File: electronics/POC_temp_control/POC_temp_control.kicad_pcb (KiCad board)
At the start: 2 copper layers, 109.2 x 78.7 mm, 177 parts, among them J1 Conn_01x02, J2 Conn_01x07, J3 Conn_01x05, J4 Conn_01x06, J5 Conn_01x02, J6 Conn_01x02, Q1 PXT8050, Q2 PXT8050, Q3 PXT8550, Q4 Q_PMOS_DUAL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

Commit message: straggling changes
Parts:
- D15: value BZX84C18 -> BZT52C18; footprint SquantorIC:SOT23-3 -> SquantorDiodes:SOD-323-nexperia-hand
- D16: value BAV70 -> BZT52C18; footprint SquantorIC:SOT23-3 -> SquantorDiodes:SOD-323-nexperia-hand
- D17: value BAS16 -> BAV70
- D18: value BZX84C18 -> BAV70
- D19: value BAV70 -> BAS316; footprint SquantorIC:SOT23-3 -> SquantorDiodes:SOD-323-nexperia-hand
- D20: value BAS16 -> BAS316; footprint SquantorIC:SOT23-3 -> SquantorDiodes:SOD-323-nexperia-hand
- Q5: value BC858B -> Q_PMOS_DUAL; footprint SquantorIC:SOT23-3 -> SquantorIC:SOIC-8
- Q6: value BC847A -> BC858B
- Q7: value Q_PMOS_DUAL -> BC858B; footprint SquantorIC:SOIC-8 -> SquantorIC:SOT23-3
- Q8: value BC858B -> BC847A
- R57: value 5K6 -> 10M
- R58: value 1M -> 5K6
- R59: value 1K5 -> 1M
- R60: value 2K2 -> 5K6
- R61: value 330 -> 1M
- R62: value 330 -> 1K5
- R63: value 6K8 -> 1K5
- R64, R65: value 10K -> 2K2
- R66: value 10K -> 330
- R67: value 10M -> 330
- R68: value 5K6 -> 330
- R69: value 1M -> 330
- R70: value 1K5 -> 6K8
- R71: value 2K2 -> 6K8
- R72, R73: value 330 -> 10K
- R74: value 6K8 -> 10K
- moved JP2 195.1 mm to (45.8, 40.5)
- moved OP1 194.9 mm to (48.1, 50.3), turned to 90 degrees
- moved C30 192.0 mm to (45.4, 44.1), turned to 90 degrees
- moved JP1 191.5 mm to (45.8, 36.9)
- moved OP2 189.8 mm to (52.9, 50.3), turned to 90 degrees
- moved R64 186.9 mm to (45.4, 47.3), turned to -90 degrees
- moved R66 181.9 mm to (50.5, 53.1), turned to -90 degrees
- moved R33 180.1 mm to (47.9, 36.5), turned to 90 degrees
- moved Q4 179.7 mm to (51.4, 38.9), turned to 90 degrees
- moved Q6 177.8 mm to (46.4, 56.3), turned to 90 degrees
- moved R62 177.5 mm to (50.5, 47.5), turned to 90 degrees
- moved R58 174.7 mm to (53.4, 45.4)
- moved R59 174.6 mm to (53.4, 43.4)
- moved R65 172.3 mm to (59.9, 46.9), turned to -90 degrees
- moved D15 171.9 mm to (47.4, 44.2), turned to 90 degrees
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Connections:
- net /Power control/AC_P1 renamed /AC_P1
- C30 pad 2: /Power control/SW_S1 -> /SW_S1
- C31 pad 1: Net-(D18-K) -> Net-(D16-K)
- C31 pad 2: /Power control/SW_S2 -> /SW_S2
- D15 pad 1: /Power control/SW_S1 -> Net-(D15-K)
- D15 pad 2: (no net) -> /SW_S1
- D16 pad 1: /Power control/SW_S1 -> Net-(D16-K)
- D16 pad 2: Net-(D16-K2) -> /SW_S2
- D17 pad 1: /Power control/GND -> /SW_S1
- D17 pad 2: (no net) -> Net-(D17-K2)
- D17 pad 3: Net-(D17-K) -> /SW_G1
- D18 pad 1: /Power control/SW_S2 -> /SW_S2
- D18 pad 2: (no net) -> Net-(D18-K2)
- D18 pad 3: Net-(D18-K) -> /SW_G2
- D19 pad 1: /Power control/SW_S2 -> Net-(D19-K)
- D19 pad 2: Net-(D19-K2) -> /GND
- D20 pad 1: /Power control/GND -> Net-(D20-K)
- D20 pad 2: (no net) -> /GND
- JP1 pad 1: /Power control/AC2 -> /AC2
- JP2 pad 1: /Power control/AC1 -> /AC1
- JP3 pad 1: /Power control/AC2 -> /AC2
- JP3 pad 2: /Power control/AC_P2 -> /AC_P2
- JP4 pad 1: /Power control/AC1 -> /AC1
- JP4 pad 2: /Power control/AC_P2 -> /AC_P2
- OP1 pad 1: Net-(Q5-C) -> Net-(Q6-C)
- OP2 pad 2: Net-(Q6-C) -> Net-(Q8-C)
- OP2 pad 3: /Power control/SW_S1 -> /SW_S1
- OP2 pad 4: Net-(D16-K2) -> Net-(D17-K2)
- OP3 pad 1: Net-(Q8-C) -> Net-(Q7-C)
- OP3 pad 4: Net-(D18-K) -> Net-(D16-K)
- OP4 pad 3: /Power control/SW_S2 -> /SW_S2
- OP4 pad 4: Net-(D19-K2) -> Net-(D18-K2)
- Q4 pad 2: /Power control/SW_G1 -> /SW_G1
- Q4 pad 3: /Power control/COM1 -> /COM1
- Q4 pad 4: /Power control/SW_G1 -> /SW_G1
- Q4 pad 5: /Power control/SW_S1 -> /SW_S1
- Q4 pad 6: /Power control/SW_S1 -> /SW_S1
- Q4 pad 7: /Power control/SW_S1 -> /SW_S1
- Q4 pad 8: /Power control/SW_S1 -> /SW_S1
- Q5 pad 1: Net-(Q5-B) -> /AC_P2
- Q5 pad 2: /Power control/VD3.3V+ -> /SW_G2
- Q5 pad 3: Net-(Q5-C) -> /COM1
- Q6 pad 2: /Power control/GND -> /VD3.3V+
- Q7 pad 1: /Power control/AC_P2 -> Net-(Q7-B)
- Q7 pad 2: /Power control/SW_G2 -> /VD3.3V+
- Q7 pad 3: /Power control/COM1 -> Net-(Q7-C)
- Q8 pad 2: /Power control/VD3.3V+ -> /GND
- Q9 pad 2: /Power control/GND -> /GND
- R33 pad 2: /Power control/COM1 -> /COM1
- R57 pad 1: /Power control/SW_G1 -> /AC_P2
- R57 pad 2: Net-(D16-K2) -> /COM1
- R58 pad 1: /Power control/SW_G1 -> /SW_G1
- R58 pad 2: /Power control/SW_S1 -> Net-(D17-K2)
- R59 pad 1: Net-(OP1-Pad3) -> /SW_G1
- R59 pad 2: Net-(D16-K2) -> /SW_S1
- R60 pad 1: Net-(D15-K) -> /SW_G2
- R60 pad 2: Net-(D17-K) -> Net-(D18-K2)
- R61 pad 1: /Power control/GND -> /SW_G2
- R61 pad 2: Net-(OP1-Pad2) -> /SW_S2
- R62 pad 1: Net-(OP2-Pad1) -> Net-(OP1-Pad3)
- R62 pad 2: /Power control/VD3.3V+ -> Net-(D17-K2)
- R63 pad 1: Net-(Q5-B) -> Net-(OP3-Pad3)
- R63 pad 2: /Power control/VD3.3V+ -> Net-(D18-K2)
- R64 pad 1: Net-(Q5-B) -> Net-(D15-K)
- R64 pad 2: /Power control/SW_LOAD_1 -> Net-(D19-K)
- R65 pad 1: Net-(Q6-B) -> Net-(D16-K)
- R65 pad 2: /Power control/SW_LOAD_1 -> Net-(D20-K)
- R66 pad 1: /Power control/SW_LOAD_1 -> /GND
- R66 pad 2: /Power control/VD3.3V+ -> Net-(OP1-Pad2)
- R67 pad 1: /Power control/AC_P2 -> Net-(OP2-Pad1)
- R67 pad 2: /Power control/COM1 -> /VD3.3V+
- R68 pad 1: /Power control/SW_G2 -> /GND
- R68 pad 2: Net-(D19-K2) -> Net-(OP3-Pad2)
- R69 pad 1: /Power control/SW_G2 -> Net-(OP4-Pad1)
- R69 pad 2: /Power control/SW_S2 -> /VD3.3V+
- R70 pad 1: Net-(OP3-Pad3) -> Net-(Q6-B)
- R70 pad 2: Net-(D19-K2) -> /VD3.3V+
- R71 pad 1: Net-(D18-K) -> Net-(Q7-B)
- R71 pad 2: Net-(D20-K) -> /VD3.3V+
- R72 pad 1: /Power control/GND -> Net-(Q6-B)
- R72 pad 2: Net-(OP3-Pad2) -> /SW_LOAD_1
- R73 pad 1: Net-(OP4-Pad1) -> Net-(Q8-B)
- R73 pad 2: /Power control/VD3.3V+ -> /SW_LOAD_1
- R74 pad 1: Net-(Q8-B) -> Net-(Q7-B)
- R74 pad 2: /Power control/VD3.3V+ -> /SW_LOAD_2
- R75 pad 1: Net-(Q8-B) -> Net-(Q9-B)
- R75 pad 2: /Power control/SW_LOAD_2 -> /SW_LOAD_2
- R76 pad 1: Net-(Q9-B) -> /SW_LOAD_1
- R76 pad 2: /Power control/SW_LOAD_2 -> /VD3.3V+
- R77 pad 1: /Power control/SW_LOAD_2 -> /SW_LOAD_2
- R77 pad 2: /Power control/VD3.3V+ -> /VD3.3V+

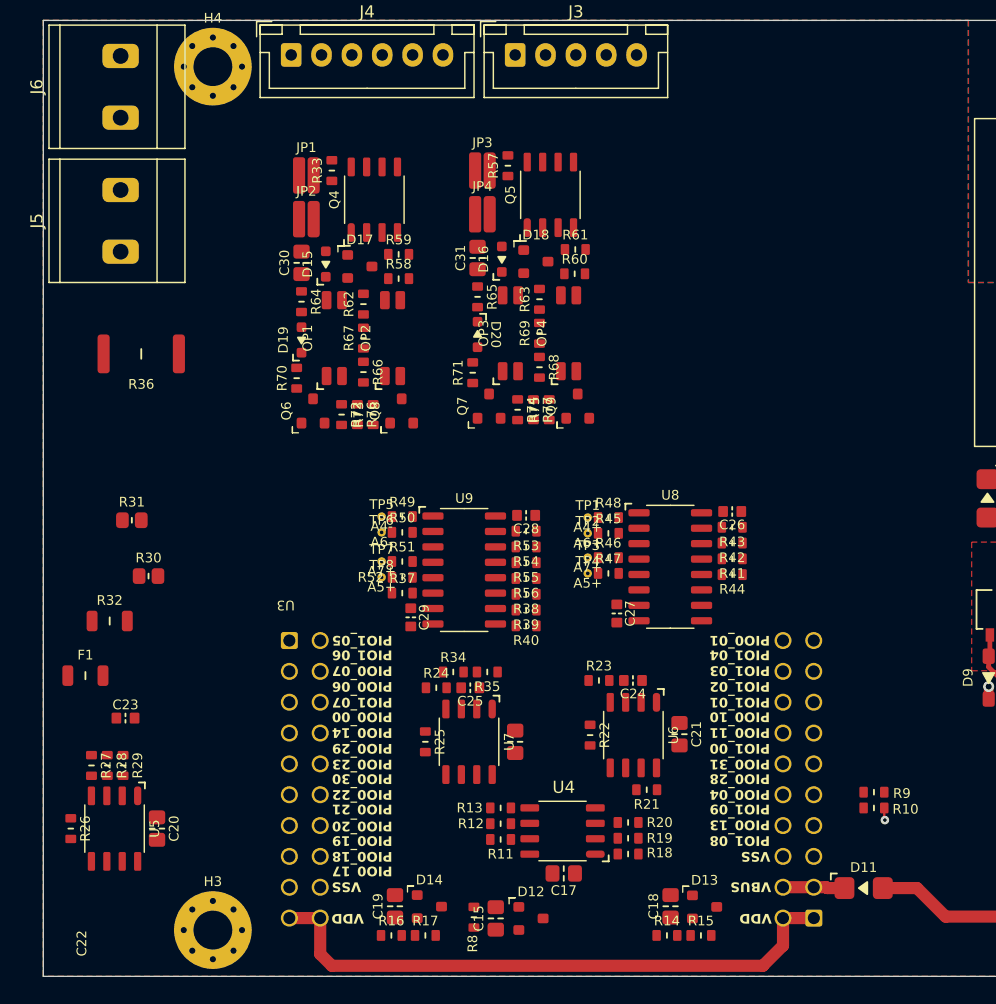
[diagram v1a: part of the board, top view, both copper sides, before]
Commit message: replaced current sense resistor, imported zerocross detector
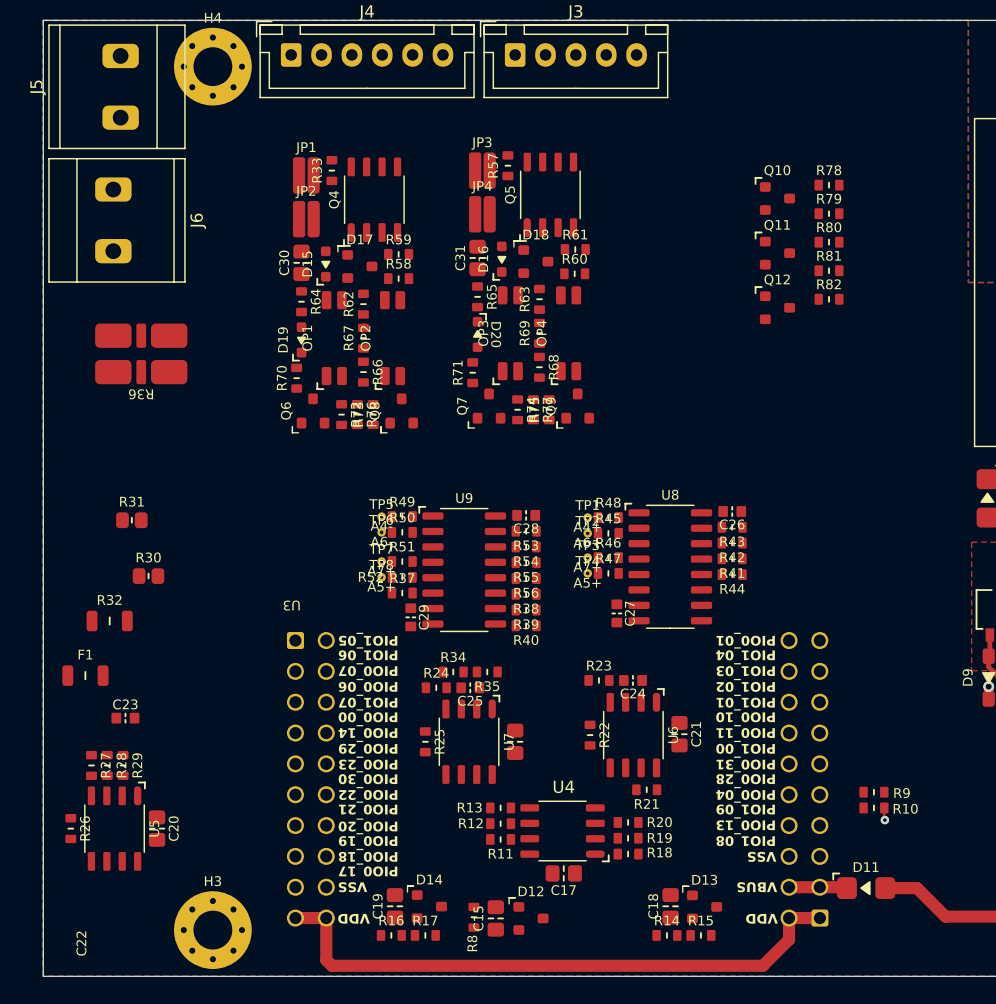
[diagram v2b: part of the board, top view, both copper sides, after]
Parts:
- added Q10: BC847A, SquantorIC:SOT23-3, F.Cu at (84.6, 38.8)
- added Q11: BC858B, SquantorIC:SOT23-3, F.Cu at (84.6, 43.3)
- added Q12: BC847A, SquantorIC:SOT23-3, F.Cu at (84.6, 47.8)
- added R78: 47K, SquantorResistor:R_0603_hand, F.Cu at (88.8, 37.7)
- added R79: 10K, SquantorResistor:R_0603_hand, F.Cu at (88.8, 40.0)
- added R80: 10K, SquantorResistor:R_0603_hand, F.Cu at (88.8, 42.4)
- added R81: 22K, SquantorResistor:R_0603_hand, F.Cu at (88.8, 44.8)
- added R82: 1M, SquantorResistor:R_0603_hand, F.Cu at (88.8, 47.1)
- R36: footprint SquantorResistor:R_2512 -> SquantorResistor:R_1225_kelvin
- moved J5 11.0 mm to (30.5, 29.6)
- moved J6 11.0 mm to (29.9, 40.6), turned to -90 degrees
- moved U3 0.50 mm to (66.5, 87.0)
- moved D11 0.20 mm to (91.9, 95.6)
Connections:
- Q5 pad 3: /COM1 -> /COM2
- R36 pad 2: /GND -> unconnected-(R36-Pad2)
- R57 pad 2: /COM1 -> /COM2

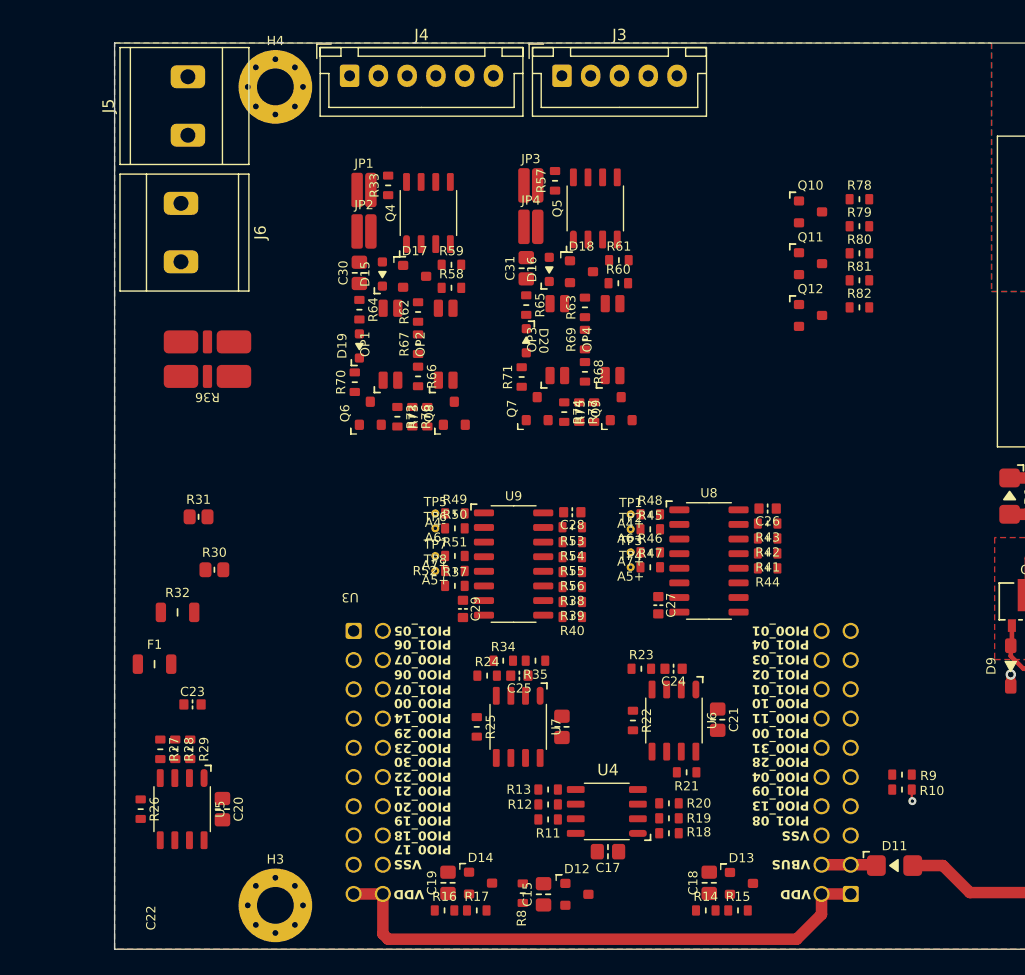
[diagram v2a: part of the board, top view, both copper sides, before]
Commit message: more schematic bits added, passes ERC, placing components and fixing silk orientations
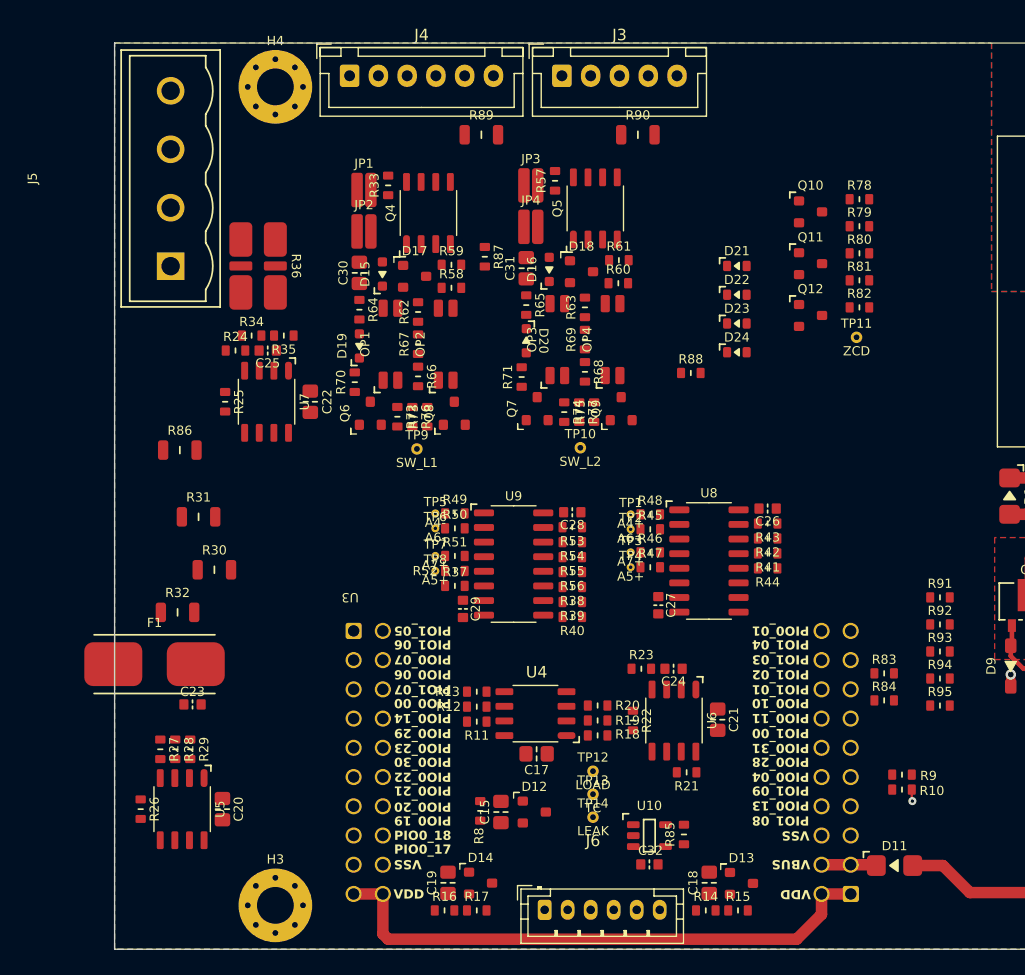
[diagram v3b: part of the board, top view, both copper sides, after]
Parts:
- added C32: 1u, SquantorCapacitor:C_0603, F.Cu at (70.6, 95.5)
- added D21: Yel, SquantorDiodes:LED_0603_hand, F.Cu at (78.2, 43.5)
- added D22: blu, SquantorDiodes:LED_0603_hand, F.Cu at (78.2, 46.0)
- added D23: blu, SquantorDiodes:LED_0603_hand, F.Cu at (78.2, 48.5)
- added D24: Yel, SquantorDiodes:LED_0603_hand, F.Cu at (78.2, 51.0)
- added R83: 3K3, SquantorResistor:R_0603_hand, F.Cu at (91.0, 78.9)
- added R84: 3K3, SquantorResistor:R_0603_hand, F.Cu at (91.0, 81.2)
- added R85: 4K7, SquantorResistor:R_0603_hand, F.Cu at (73.6, 92.9)
- added R86: 0R, SquantorResistor:R_1206, F.Cu at (29.8, 59.5)
- added R87: 10k, SquantorResistor:R_0603_hand, F.Cu at (56.3, 42.7)
- added R88: 10k, SquantorResistor:R_0603_hand, F.Cu at (74.2, 52.8)
- added R89: 0R, SquantorResistor:R_1206, F.Cu at (56.0, 32.1)
- added R90: 0R, SquantorResistor:R_1206, F.Cu at (69.6, 32.1)
- added R91: 10K, SquantorResistor:R_0603_hand, F.Cu at (95.8, 72.3)
- added R92: 10K, SquantorResistor:R_0603_hand, F.Cu at (95.8, 74.7)
- added R93: 10K, SquantorResistor:R_0603_hand, F.Cu at (95.8, 77.0)
- added R94: 10K, SquantorResistor:R_0603_hand, F.Cu at (95.8, 79.3)
- added R95: 10K, SquantorResistor:R_0603_hand, F.Cu at (95.8, 81.7)
- added TP10: SW_L2, SquantorTestPoints:TestPoint_hole_H05R10, F.Cu at (64.6, 59.3)
- added TP11: ZCD, SquantorTestPoints:TestPoint_hole_H05R10, F.Cu at (88.6, 49.7)
- added TP12: LOAD, SquantorTestPoints:TestPoint_hole_H05R10, F.Cu at (65.7, 87.4)
- added TP13: TC, SquantorTestPoints:TestPoint_hole_H05R10, F.Cu at (65.7, 89.4)
- added TP14: LEAK, SquantorTestPoints:TestPoint_hole_H05R10, F.Cu at (65.7, 91.4)
- added TP9: SW_L1, SquantorTestPoints:TestPoint_hole_H05R10, F.Cu at (50.4, 59.4)
- added U10: ~, SquantorIC:SOT23-5-Microchip-OT, F.Cu at (70.6, 93.0)
- F1: footprint SquantorResistor:R_1206 -> SquantorFuse:FH_XF-155
- J5: value Conn_01x02 -> Conn_01x04; footprint SquantorPhoenixContact:MKDS_2conn_508pitch_1711725 -> SquantorConnectors:phoenix-MSTBVA-1755752-4p-508-str
- J6: value Conn_01x02 -> Conn_01x06; footprint SquantorPhoenixContact:MKDS_2conn_508pitch_1711725 -> Connector_JST:JST_PH_B6B-PH-K_1x06_P2.00mm_Vertical
- R30, R31: footprint SquantorResistor:R_0805+0603 -> SquantorResistor:R_1206
- moved J6 66.8 mm to (61.5, 99.5), turned to 0 degrees
- moved C22 35.7 mm to (41.1, 55.3)
- moved R25 35.7 mm to (33.7, 55.3)
- moved R34 35.7 mm to (36.0, 49.5)
- moved R35 35.7 mm to (38.8, 49.5)
- moved U7 35.7 mm to (37.3, 55.3)
- moved C25 35.7 mm to (37.4, 50.9)
- moved R24 35.7 mm to (34.6, 50.9)
- moved C17 10.5 mm to (60.8, 85.9)
- moved R18 10.5 mm to (66.1, 84.3)
- moved R19 10.5 mm to (66.1, 83.0)
- moved R20 10.5 mm to (66.1, 81.7)
- moved U4 10.5 mm to (60.7, 82.4)
- moved R11 10.5 mm to (55.6, 83.1)
- moved R12 10.5 mm to (55.6, 81.8)
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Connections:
- C10 pad 1: /+5VD -> /VD5V+
- C12 pad 1: /+5VD -> /VD5V+
- C14 pad 1: /+5VD -> /VD5V+
- C16 pad 1: /+5VD -> /VD5V+
- D11 pad 2: /+5VD -> /VD5V+
- H3 pad 1: (no net) -> /CASE_GND
- J3 pad 3: /LOAD2 -> /LOAD1
- J4 pad 5: /LOAD1 -> /LOAD2
- J5 pad 1: /AC2 -> /GND
- J6 pad 1: /AC1 -> /VD5V+
- J6 pad 2: /GND -> /VD3.3V+
- L1 pad 1: /+5VD -> /VD5V+
- Q11 pad 3: Net-(Q11-C) -> /ZCD
- R3 pad 1: /+5VD -> /VD5V+
- R34 pad 1: /GND -> /GND_SEN
- R35 pad 1: /LOAD -> /LOAD_SEN
- R36 pad 2: unconnected-(R36-Pad2) -> /LOAD_SEN
- R36 pad 3: unconnected-(R36-Pad3) -> /GND_SEN
- R80 pad 2: Net-(Q11-C) -> /ZCD
- U3 pad 11: unconnected-(U3A-PIO0_28-Pad11) -> /!UI_INT
- U3 pad 14: unconnected-(U3A-PIO0_11-Pad14) -> /I2C_SDA
- U3 pad 15: unconnected-(U3A-PIO0_10-Pad15) -> /I2C_SCL
- U3 pad 35: unconnected-(U3B-PIO0_17-Pad35) -> /ZCD
